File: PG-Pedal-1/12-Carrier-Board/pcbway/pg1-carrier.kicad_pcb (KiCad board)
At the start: 2 copper layers, 111 x 42.2 mm, 98 parts, among them J1 line in, J10 seed3 in + power, J11 seed3 out, J19 pg-hp, J2 line out, J20 pg-line, J3 no amp, J4 phones, J9 9V in, U1 LP2985-33, U4 NE5532, U5 NE5532, U6 NE5532, U7 TPA6139A2, U8 TPA6139A2, U9 TLV7031

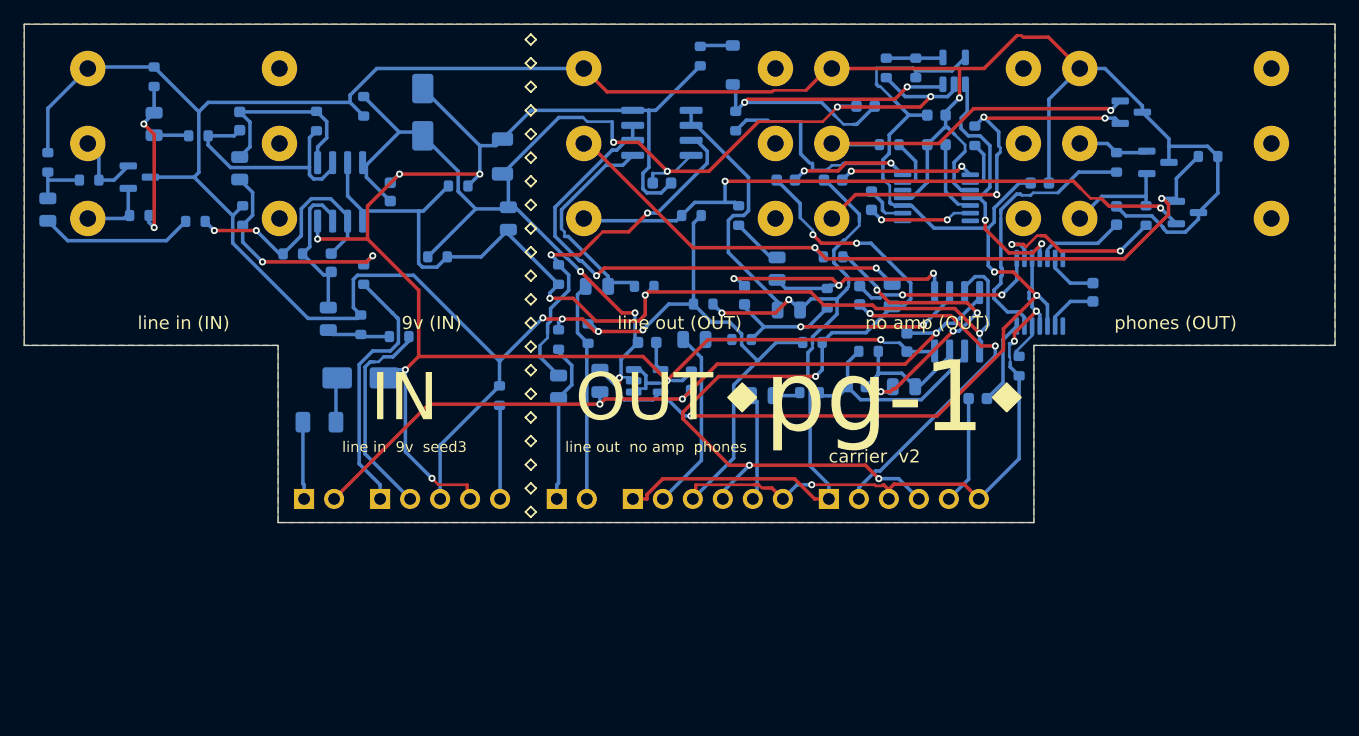
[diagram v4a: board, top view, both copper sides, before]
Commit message: v3 isolated carrier board: one isolated stereo in + out (TLV320AIC3204 behind ISO7741 / ISO1540 / B0505S), analog centre-click gain knobs, firmware SAI2 + codec, face print and drill to match
Co-Authored-By: Claude Opus 5.5 <noreply@anthropic.com>
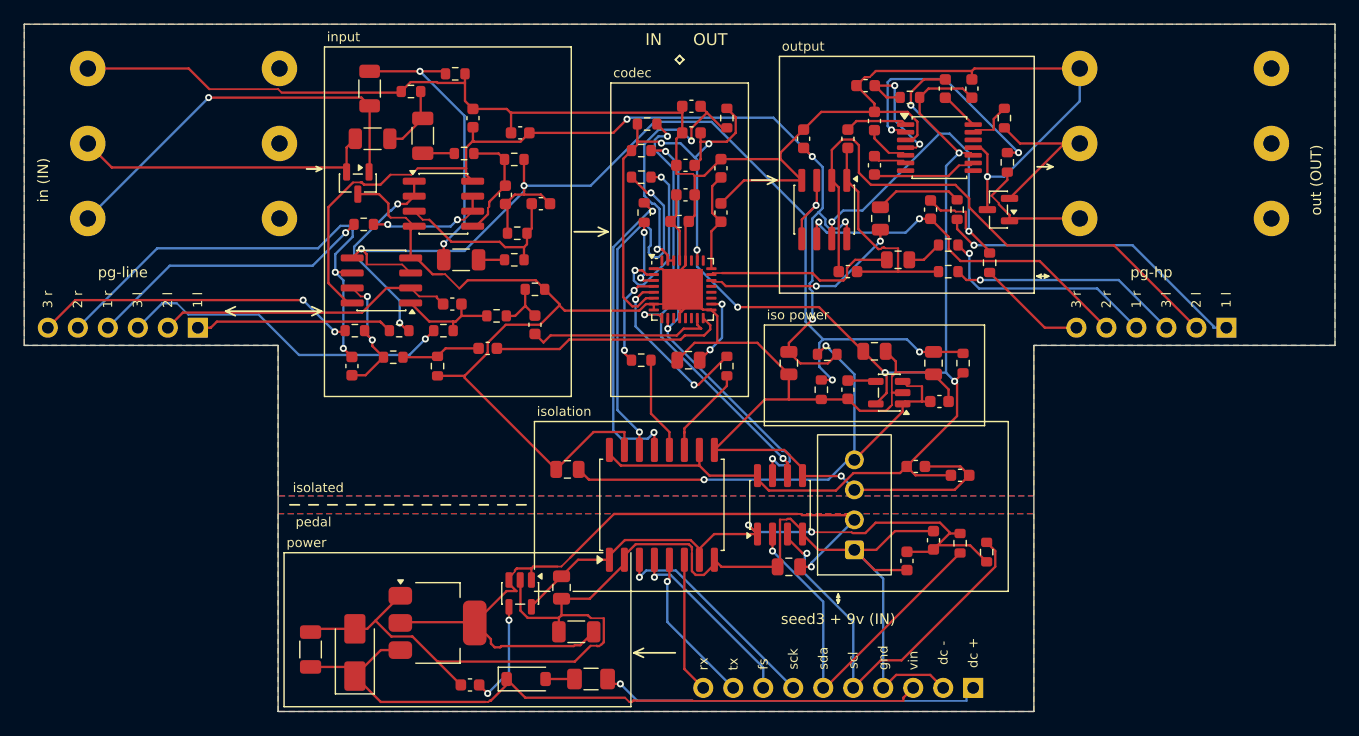
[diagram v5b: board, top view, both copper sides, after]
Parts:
- removed C34, C35, C37: 10uF 25V, C_0805_2012Metric
- removed C36: 47pF C0G, C_0603_1608Metric
- removed C38, C39, C63, C64, C65: 1uF, C_0603_1608Metric
- removed C4: 4.7uF, C_0805_2012Metric
- removed C66, C67, C68: 100nF, C_0603_1608Metric
- removed D50: 1N4148W, D_SOD-123
- removed D63, D64: PESD15VL2BT, SOT-23
- removed J11: seed3 out, PinHeader_1x02_P2.54mm_Horizontal
- removed J3: no amp, Jack_6.35mm_Neutrik_NMJ6HCD2_Horizontal
- removed J4: phones, Jack_6.35mm_Neutrik_NMJ6HCD2_Horizontal
- removed J9: 9V in, PinHeader_1x02_P2.54mm_Horizontal
- removed R1, R2: 10k, R_0603_1608Metric
- removed R15, R16, R17, R19, R21, R24, R39, R53: 100k, R_0603_1608Metric
- removed R18, R38: 51k, R_0603_1608Metric
- removed R20: 100, R_0603_1608Metric
- removed R22, R23: 1, R_0603_1608Metric
- removed R71: 0, R_0603_1608Metric
- removed U6: NE5532, SOIC-8_3.9x4.9mm_P1.27mm
- added C20: 100nF, C_0603_1608Metric, F.Cu at (103.5, 45.8)
- added C21: 1uF, C_0603_1608Metric, F.Cu at (100.0, 46.5)
- added C22: 100nF, C_0603_1608Metric, F.Cu at (100.5, 44.2)
- added C23: 1uF, C_0603_1608Metric, F.Cu at (100.5, 41.8)
- added C24: 100nF, C_0603_1608Metric, F.Cu at (101.0, 39.0)
- added C25: 100nF, C_0603_1608Metric, F.Cu at (101.0, 36.8)
- added C26: 100nF, C_0603_1608Metric, F.Cu at (82.5, 37.8)
- added C27: 100nF, C_0603_1608Metric, F.Cu at (86.5, 39.0)
- added C28: 100nF, C_0603_1608Metric, F.Cu at (110.5, 39.5)
- added C40: 47nF C0G, C_1206_3216Metric, F.Cu at (78.2, 39.2)
- added C41: 100pF C0G, C_0603_1608Metric, F.Cu at (85.2, 44.2)
- added C42: 1uF, C_0603_1608Metric, F.Cu at (83.8, 57.2)
- added C43: 100pF C0G, C_0603_1608Metric, F.Cu at (72.2, 58.8)
- added C51: 1uF, C_0603_1608Metric, F.Cu at (114.2, 39.5)
- added C52: 100pF C0G, C_0603_1608Metric, F.Cu at (114.2, 50.8)
- added C7: 10uF 25V, C_0805_2012Metric, F.Cu at (109.2, 75.8)
- added C70: 1uF, C_0603_1608Metric, F.Cu at (116.5, 41.8)
- added C71: 1uF, C_0603_1608Metric, F.Cu at (116.5, 38.0)
- added C72: 1uF, C_0603_1608Metric, F.Cu at (124.8, 35.2)
- added C73: 1uF, C_0603_1608Metric, F.Cu at (115.8, 35.0)
- added C8: 10uF 25V, C_0805_2012Metric, F.Cu at (90.5, 67.5)
- added C9: 100nF, C_0603_1608Metric, F.Cu at (119.2, 75.2)
- added R3: 4.7k, R_0603_1608Metric, F.Cu at (126.0, 74.5)
- added R4: 4.7k, R_0603_1608Metric, F.Cu at (123.8, 73.8)
- added R45: 10k, R_0603_1608Metric, F.Cu at (79.5, 58.8)
- added R46: 220, R_0603_1608Metric, F.Cu at (73.2, 46.8)
- added R47: 220, R_0603_1608Metric, F.Cu at (72.5, 55.8)
- added R5: 10, R_0603_1608Metric, F.Cu at (112.5, 57.8)
- added R6: 10k, R_0603_1608Metric, F.Cu at (124.0, 58.5)
- added R61: 1k, R_0603_1608Metric, F.Cu at (122.8, 48.5)
- added R62: 1k, R_0603_1608Metric, F.Cu at (126.2, 50.0)
- added R7: 10k, R_0603_1608Metric, F.Cu at (112.0, 60.8)
- added R8: 10k, R_0603_1608Metric, F.Cu at (104.0, 37.8)
- added R9: 4.7k, R_0603_1608Metric, F.Cu at (97.2, 38.2)
- added U10: TPA6139A2, TSSOP-14_4.4x5mm_P0.65mm, F.Cu at (122.0, 40.2)
- added U11: OPA1652, SOIC-8_3.9x4.9mm_P1.27mm, F.Cu at (74.8, 51.5)
- added U12: OPA1652, SOIC-8_3.9x4.9mm_P1.27mm, F.Cu at (112.2, 45.5)
- added U2: LP2985-33, SOT-23-5, F.Cu at (86.5, 78.0)
- added U3: B0505S-1WR3, DCDC_SIP4_B0505S, F.Cu at (114.8, 74.3)
- C1, C17, C19, C31, C61, D2, D61, D62, F1, J19, J20: moved to F.Cu
- C10, C12: value 10uF 25V -> 100nF; footprint C_0805_2012Metric -> C_0603_1608Metric; moved to F.Cu
- C11: value 100pF C0G -> 100nF; moved to F.Cu
- C13: value 10uF 25V -> 10nF; footprint C_0805_2012Metric -> C_0603_1608Metric; moved to F.Cu
- C14: value 10uF 25V -> 4.7uF; moved to F.Cu
- C15, C32: value 10uF 25V -> 1uF; footprint C_0805_2012Metric -> C_0603_1608Metric; moved to F.Cu
- C16: value 47pF C0G -> 10uF 25V; footprint C_0603_1608Metric -> C_0805_2012Metric; moved to F.Cu
- C18: value 1uF -> 10uF 25V; footprint C_0603_1608Metric -> C_0805_2012Metric; moved to F.Cu
- C2: footprint C_0805_2012Metric -> C_1206_3216Metric; moved to F.Cu
- C3: value 10nF -> 4.7uF; footprint C_0603_1608Metric -> C_0805_2012Metric; moved to F.Cu
- C30: value 10uF 25V -> 47nF C0G; footprint C_0805_2012Metric -> C_1206_3216Metric; moved to F.Cu
- C33: value 10uF 25V -> 100pF C0G; footprint C_0805_2012Metric -> C_0603_1608Metric; moved to F.Cu
- C5: value 1uF -> 10nF; moved to F.Cu
- C50, C60: value 1uF -> 4.7uF; footprint C_0603_1608Metric -> C_0805_2012Metric; moved to F.Cu
- C62: value 1uF -> 100pF C0G; moved to F.Cu
- D1: value SS34 -> B5819W; footprint D_SMA -> D_SOD-123; moved to F.Cu
- J1: value line in -> in; footprint Jack_6.35mm_Neutrik_NMJ6HCD2_Horizontal -> Jack_6.35mm_Neutrik_NMJ6HFD2_Horizontal
- J10: value seed3 in + power -> seed3 + 9v; footprint PinHeader_1x05_P2.54mm_Horizontal -> PinHeader_1x10_P2.54mm_Horizontal; moved to F.Cu
- J2: value line out -> out; footprint Jack_6.35mm_Neutrik_NMJ6HCD2_Horizontal -> Jack_6.35mm_Neutrik_NMJ6HFD2_Horizontal
- R10: value 1k -> 4.7k; moved to F.Cu
- R11: value 20k -> 33; moved to F.Cu
- R12: value 10k -> 33; moved to F.Cu
- R13: value 100 -> 33; moved to F.Cu
- R14: value 100k -> 33; moved to F.Cu
- R30: footprint R_0603_1608Metric -> R_1206_3216Metric; moved to F.Cu
- R31: value 20k -> 1M; moved to F.Cu
- R32: value 10k -> 1M; moved to F.Cu
- R33: value 100 -> 1M; moved to F.Cu
- R34, R44: value 100k -> 20k; moved to F.Cu
- R35: value 100k -> 10k; moved to F.Cu
- R36, R37: value 100k -> 220; moved to F.Cu
- R40: value 100 -> 1k; footprint R_0603_1608Metric -> R_1206_3216Metric; moved to F.Cu
- R41: value 100k -> 1M; moved to F.Cu
- R42, R43: value 1 -> 1M; moved to F.Cu
- R50: value 470k -> 1; moved to F.Cu
- R51: value 10k -> 1k; moved to F.Cu
- R52: value 100k -> 1k; moved to F.Cu
- R60: value 11.5k 1% -> 1; moved to F.Cu
- R70: value 0 -> 470k; moved to F.Cu
- U1: value LP2985-33 -> AMS1117-5.0; footprint SOT-23-5 -> SOT-223-3_TabPin2; moved to F.Cu
- U4: value NE5532 -> ISO7741; footprint SOIC-8_3.9x4.9mm_P1.27mm -> SOIC-16W_7.5x10.3mm_P1.27mm; moved to F.Cu
- U5: value NE5532 -> ISO1540; moved to F.Cu
- U7: value TPA6139A2 -> LP2985-33; footprint TSSOP-14_4.4x5mm_P0.65mm -> SOT-23-5; moved to F.Cu
- U8: value TPA6139A2 -> OPA1652; footprint TSSOP-14_4.4x5mm_P0.65mm -> SOIC-8_3.9x4.9mm_P1.27mm; moved to F.Cu
- U9: value TLV7031 -> TLV320AIC3204; footprint SOT-23-5 -> Texas_RHB0032E_VQFN-32-1EP_5x5mm_P0.5mm_EP3.45x3.45mm; moved to F.Cu
- moved C10 70.7 mm to (120.0, 67.2), turned to 0 degrees
- moved C11 68.6 mm to (121.5, 73.5)
- moved R41 67.7 mm to (77.2, 35.5), turned to 180 degrees
- moved C12 66.3 mm to (123.8, 68.0), turned to 0 degrees
- moved J10 52.7 mm to (124.9, 86.0)
- moved U8 51.1 mm to (80.0, 45.0), turned to 0 degrees
- moved R43 51.0 mm to (86.0, 41.2), turned to 0 degrees
- moved R70 46.3 mm to (119.5, 36.0), turned to 180 degrees
- moved D2 46.1 mm to (72.5, 83.0), turned to 90 degrees
- moved C1 44.8 mm to (68.8, 82.8), turned to 90 degrees
- moved R14 42.9 mm to (104.0, 58.8), turned to -90 degrees
- moved R10 42.9 mm to (96.8, 40.5)
- moved J2 42.0 mm to (133.9, 46.2)
- moved R40 40.3 mm to (74.0, 39.5), turned to 0 degrees
- moved J20 39.6 mm to (59.2, 55.5)
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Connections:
- C10 pad 1: IN_B_L -> ISO3V3
- C10 pad 2: IN_A_L -> IGND
- C11 pad 1: IN_N_L -> +3V3
- C11 pad 2: IN_O_L -> GND
- C12 pad 1: IN_O_L -> ISO3V3
- C12 pad 2: SEED_IN_RAW_L -> IGND
- C13 pad 1: OB_P_L -> IBYP
- C13 pad 2: SEED_OUT_L -> IGND
- C14 pad 1: OB_O_L -> ISO3V3
- C14 pad 2: BUS_L -> IGND
- C15 pad 1: LO_A_L -> ISO5V_RAW
- C15 pad 2: LINE_W_L -> IGND
- C16 pad 1: LO_N_L -> ISO5V
- C16 pad 2: LO_O_L -> IGND
- C17 pad 1: LO_O_L -> IBIAS
- C17 pad 2: LO_C_L -> IGND
- C18 pad 1: BUS_L -> REF
- C18 pad 2: NA_IN_L -> IGND
- C19 pad 1: HP_W_L -> AVDD
- C19 pad 2: HP_IN_L -> IGND
- C2 pad 1: VREF -> +5V
- C3 pad 1: BYP -> +3V3
- C30 pad 1: IN_B_R -> IN_A_L
- C30 pad 2: IN_A_R -> IN_B_L
- C31 pad 1: IN_N_R -> IN_C_L
- C31 pad 2: IN_O_R -> IBIAS
- C32 pad 1: IN_O_R -> IN_E_L
- C32 pad 2: SEED_IN_RAW_R -> CIN2_L
- C33 pad 1: OB_P_R -> GIN_W_L
- C33 pad 2: SEED_OUT_R -> IN_G_L
- C5 pad 1: +9V -> PBYP
- C50 pad 1: EN_RC -> LO_L
- C50 pad 2: GND -> OUT_A_L
- C60 pad 1: NA_CP -> LO_R
- C60 pad 2: NA_CN -> OUT_A_R
- C61 pad 1: AGND -> OUT_G_R
- C61 pad 2: NA_VSS -> HPIN_R
- C62 pad 1: HP_CP -> GOUT_W_R
- C62 pad 2: HP_CN -> OUT_G_R
- D61 pad 3: AGND -> IGND
- D62 pad 1: JLO_L -> JOUT_L
- D62 pad 2: JLO_R -> JOUT_R
- D62 pad 3: AGND -> IGND
- J1 pad S: AGND -> IGND
- J10 pad 1: SEED_IN_L -> +9V_RAW
- J10 pad 2: SEED_IN_R -> GND
- J10 pad 3: AGND -> +9V
- J10 pad 4: +9V -> GND
- J10 pad 5: DGND -> SEED_SCL
- J19 pad 1: BUS_L -> GOUT_A_L
- J19 pad 2: HP_W_L -> GOUT_W_L
- J19 pad 3: AGND -> GOUT_B_L
- J19 pad 4: BUS_R -> GOUT_A_R
- J19 pad 5: HP_W_R -> GOUT_W_R
- J19 pad 6: AGND -> GOUT_B_R
- J2 pad R: JLO_R -> JOUT_R
- J2 pad S: AGND -> IGND
- J2 pad T: JLO_L -> JOUT_L
- J20 pad 1: BUS_L -> GIN_A_L
- J20 pad 2: LINE_W_L -> GIN_W_L
- J20 pad 3: AGND -> GIN_B_L
- J20 pad 4: BUS_R -> GIN_A_R
- J20 pad 5: LINE_W_R -> GIN_W_R
- J20 pad 6: AGND -> GIN_B_R
- R10 pad 1: JIN_L -> ISO3V3
- R10 pad 2: IN_A_L -> ISDA
- R11 pad 1: IN_B_L -> BCLK_X
- R11 pad 2: IN_N_L -> BCLK
- R12 pad 1: IN_N_L -> WCLK_X
- R12 pad 2: IN_O_L -> WCLK
- R13 pad 1: SEED_IN_RAW_L -> DIN_X
- R13 pad 2: SEED_IN_L -> DIN
- R14 pad 1: SEED_IN_RAW_L -> DOUT
- R14 pad 2: AGND -> DOUT_X
- R30 pad 1: JIN_R -> JIN_L
- R30 pad 2: IN_A_R -> IN_A_L
- R31 pad 1: IN_B_R -> IN_A_L
- R31 pad 2: IN_N_R -> IGND
- R32 pad 1: IN_N_R -> IN_B_L
- R32 pad 2: IN_O_R -> IN_C_L
- R33 pad 1: SEED_IN_RAW_R -> IN_C_L
- R33 pad 2: SEED_IN_R -> IBIAS
- R34 pad 1: SEED_IN_RAW_R -> IN_G_L
- R34 pad 2: AGND -> IN_E_L
- R35 pad 1: OB_P_R -> IN_E_L
- R35 pad 2: VREF -> IGND
- R36 pad 1: SEED_OUT_R -> IN_D_L
- R36 pad 2: AGND -> GIN_A_L
- R37 pad 1: BUS_R -> GIN_B_L
- R37 pad 2: AGND -> IN_G_L
- R40 pad 1: LO_C_R -> JIN_R
- R40 pad 2: JLO_R -> IN_A_R
- R41 pad 1: JLO_R -> IN_A_R
- R41 pad 2: AGND -> IGND
- R42 pad 1: NA_O_R -> IN_B_R
- R42 pad 2: JNA_R -> IN_C_R
- R43 pad 1: HP_O_R -> IN_C_R
- R43 pad 2: JHP_R -> IBIAS
- R44 pad 1: IN_A_R -> IN_G_R
- R44 pad 2: AGND -> IN_E_R
- R50 pad 1: +3V3A -> HPO_L
- R50 pad 2: EN_RC -> JOUT_L
- R51 pad 1: +9V -> OUT_A_L
- R51 pad 2: +9V_SENSE -> GOUT_A_L
- R52 pad 1: +3V3A -> GOUT_B_L
- R52 pad 2: EN_REF -> OUT_G_L
- R60 pad 1: HP_GAIN -> HPO_R
- R60 pad 2: AGND -> JOUT_R
- R70 pad 1: GND -> ISO3V3
- R70 pad 2: AGND -> HP_ON
- U1 pad 1: +9V -> GND
- U1 pad 2: GND -> +5V
- U4 pad 1: IN_O_L -> +3V3
- U4 pad 2: IN_N_L -> GND
- U4 pad 3: VREF -> SEED_SCK
- U4 pad 4: GND -> SEED_FS
- U4 pad 5: VREF -> SEED_TX
- U4 pad 6: IN_N_R -> SEED_RX
- U4 pad 7: IN_O_R -> +3V3
- U4 pad 8: +9V -> GND
- U5 pad 1: OB_O_L -> +3V3
- U5 pad 2: OB_O_L -> SEED_SDA
- U5 pad 3: OB_P_L -> SEED_SCL
- U5 pad 5: OB_P_R -> IGND
- U5 pad 6: OB_O_R -> ISCL
- U5 pad 7: OB_O_R -> ISDA
- U5 pad 8: +9V -> ISO3V3
- U7 pad 1: NA_IN_L -> ISO5V_RAW
- U7 pad 2: NA_O_L -> IGND
- U7 pad 3: AGND -> ISO5V_RAW
- U7 pad 4: MUTE_N -> IBYP
- U7 pad 5: NA_VSS -> ISO3V3
- U8 pad 1: HP_IN_L -> IN_D_L
- U8 pad 2: HP_O_L -> IN_D_L
- U8 pad 3: AGND -> IN_C_L
- U8 pad 4: MUTE_N -> IGND
- U8 pad 5: HP_VSS -> IN_C_R
- U8 pad 6: HP_CN -> IN_D_R
- U8 pad 7: (no net) -> IN_D_R
- U8 pad 8: (no net) -> ISO5V
- U9 pad 1: MUTE_N -> IGND
- U9 pad 2: GND -> BCLK
- U9 pad 3: EN_RC -> WCLK
- U9 pad 4: EN_REF -> DIN
- U9 pad 5: +3V3A -> DOUT
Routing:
- net AGND: track 336.9 -> 0.00 mm, vias 8 -> 0
- net IGND: track 0.00 -> 300.6 mm, vias 0 -> 2
- net ISO3V3: track 0.00 -> 148.1 mm, vias 0 -> 7
- net +3V3A: track 112.0 -> 0.00 mm, vias 3 -> 0
- net IBIAS: track 0.00 -> 97.5 mm, vias 0 -> 5
- net ISO5V: track 0.00 -> 87.3 mm, vias 0 -> 4
- net +9V: track 146.5 -> 59.4 mm, vias 7 -> 0
- net VREF: track 85.8 -> 0.00 mm, vias 3 -> 0
- net BUS_R: track 69.0 -> 0.00 mm, vias 5 -> 0
- net GND: track 181.9 -> 114.7 mm, vias 10 -> 0
- net JLO_R: track 63.8 -> 0.00 mm, vias 2 -> 0
- net +5V: track 0.00 -> 63.3 mm, vias 0 -> 1
- net BUS_L: track 62.3 -> 0.00 mm, vias 2 -> 0
- net JLO_L: track 55.5 -> 0.00 mm, vias 2 -> 0
- net +3V3: track 0.00 -> 52.8 mm, vias 0 -> 2
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- added copper zone on B.Cu, net GND
- added copper zone on F.Cu, net GND
- added copper zone on B.Cu, net IGND
- added copper zone on F.Cu, net IGND
- removed copper zone on B.Cu, net AGND
- removed copper zone on F.Cu, net AGND
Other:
- board size 111 x 42.2 mm -> 111 x 58.2 mm
- board text added: "1 l"
- board text added: "1 r"
- board text added: "2 l"
- board text added: "2 r"
- board text added: "3 l"
- board text added: "3 r"
- board text added: "codec"
- board text added: "dc +"
- board text added: "dc -"
- board text added: "fs"
- board text added: "in (IN)"
- board text added: "input"
- board text added: "iso power"
- board text added: "isolated"
- board text added: "isolation"
- board text added: "out (OUT)"
- board text added: "output"
- board text added: "pedal"
- board text added: "power"
- board text added: "rx"
- board text added: "sck"
- board text added: "scl"
- board text added: "sda"
- board text added: "seed3 + 9v (IN)"
- board text added: "tx"
- board text added: "vin"
- board text removed: "+"
- board text removed: "-"
- board text removed: "9v"
- board text removed: "9v (IN)"
- board text removed: "agnd"
- board text removed: "bus l"
- board text removed: "bus r"
- board text removed: "carrier v2"
- board text removed: "dgnd"
- board text removed: "hp l"
- board text removed: "hp r"
- board text removed: "in l"
- board text removed: "in r"
- board text removed: "line in (IN)"
- board text removed: "line in 9v seed3"
- board text removed: "line l"
- board text removed: "line out (OUT)"
- board text removed: "line out no amp phones"
- board text removed: "line r"
- board text removed: "no amp (OUT)"
- board text removed: "out l"
- board text removed: "out r"
- board text removed: "pg-1"
- board text removed: "phones (OUT)"
- board text removed: "seed3 (IN)"
- board text removed: "seed3 (OUT)"

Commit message: Carrier: analog fx (MCP4461 level + low-pass, TLV9062), expansion header + left-wall bay, re-route
Co-Authored-By: Claude Opus 5.5 <noreply@anthropic.com>
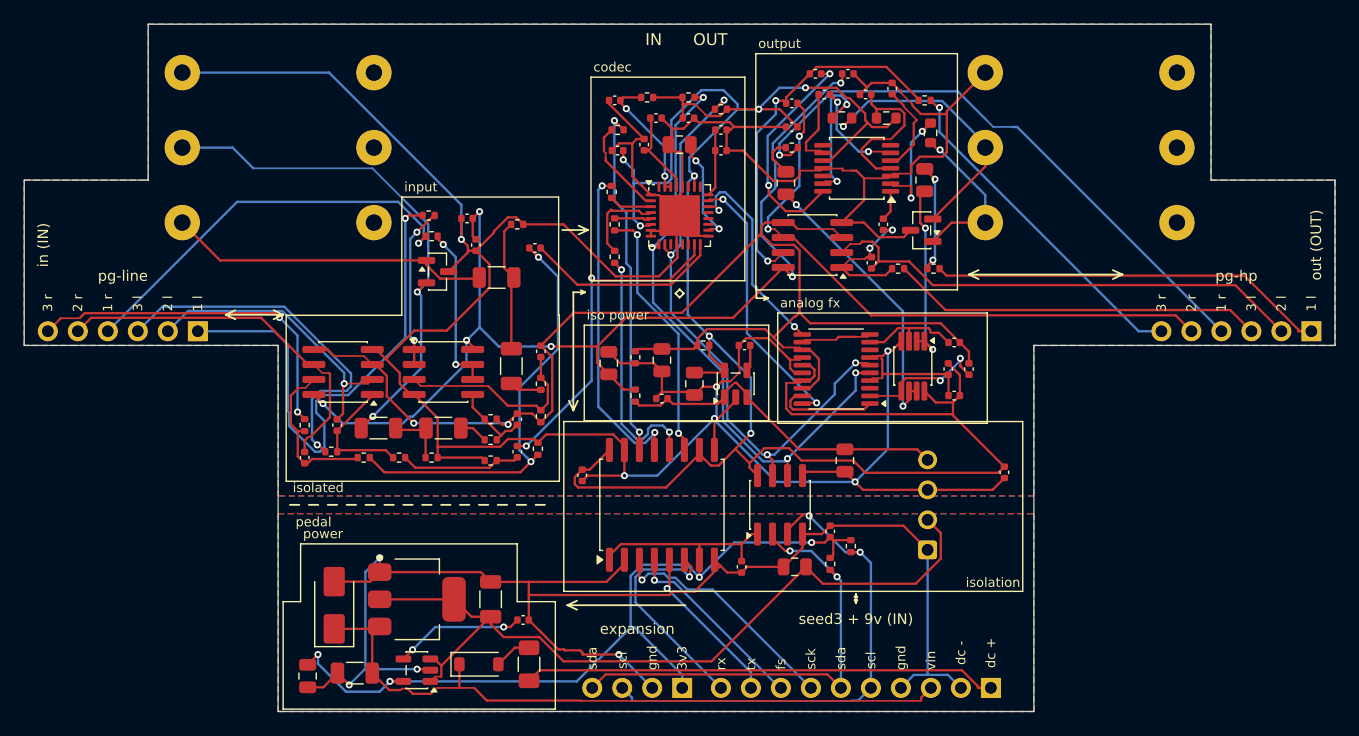
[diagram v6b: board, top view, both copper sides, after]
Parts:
- added C74: 10nF C0G, C_0402_1005Metric, F.Cu at (123.2, 56.8)
- added C75: 100nF, C_0402_1005Metric, F.Cu at (122.8, 59.0)
- added C76: 10nF C0G, C_0402_1005Metric, F.Cu at (124.5, 59.0)
- added C78: 100nF, C_0402_1005Metric, F.Cu at (123.2, 61.2)
- added J21: expansion, PinHeader_1x04_P2.54mm_Horizontal, F.Cu at (100.2, 86.0)
- added U13: MCP4461-103, TSSOP-20_4.4x6.5mm_P0.65mm, F.Cu at (113.2, 59.0)
- added U15: TLV9062, VSSOP-8_3x3mm_P0.65mm, F.Cu at (119.8, 58.8)
- C10, C11, C12, C13, C15, C19, C20, C21, C22, C23, C24, C25, C26, C27, C28, C31, C32, C33, C41, C42, C43, C5, C51, C52, C61, C62, C70, C71, C72, C73, C9: footprint C_0603_1608Metric -> C_0402_1005Metric
- R10, R11, R12, R13, R14, R3, R31, R32, R33, R34, R35, R36, R37, R4, R41, R42, R43, R44, R45, R46, R47, R5, R51, R52, R6, R61, R62, R7, R8, R9: footprint R_0603_1608Metric -> R_0402_1005Metric
- moved R41 31.0 mm to (79.0, 66.5), turned to 0 degrees
- moved C10 28.3 mm to (91.8, 68.0), turned to -90 degrees
- moved C40 24.8 mm to (80.0, 64.0), turned to 0 degrees
- moved R40 24.5 mm to (74.5, 64.0)
- moved R42 24.4 mm to (84.0, 65.0)
- moved C8 23.5 mm to (114.0, 66.8), turned to -90 degrees
- moved C15 23.5 mm to (98.5, 61.5), turned to 180 degrees
- moved C17 23.0 mm to (98.5, 58.2)
- moved C3 22.8 mm to (68.5, 85.0)
- moved R43 22.1 mm to (84.0, 63.2)
- moved R6 22.1 mm to (102.0, 57.0), turned to 180 degrees
- moved R30 19.3 mm to (84.5, 51.2), turned to 0 degrees
- moved C41 19.0 mm to (86.2, 63.2), turned to 90 degrees
- moved C18 18.3 mm to (100.0, 40.0)
- moved R5 16.6 mm to (96.2, 61.2), turned to 90 degrees
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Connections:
- C50 pad 1: LO_L -> ABUF_L
- C60 pad 1: LO_R -> ABUF_R
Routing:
- net ISO3V3: track 148.1 -> 182.8 mm
- net +3V3: track 52.8 -> 84.9 mm, vias 2 -> 4
- net GOUT_A_R: track 19.3 -> 50.5 mm
- net IN_E_R: track 6.71 -> 36.2 mm, vias 0 -> 2
- net GIN_A_L: track 16.8 -> 44.7 mm, vias 0 -> 1
- net ABUF_R: track 0.00 -> 24.2 mm, vias 0 -> 2
- net GOUT_W_R: track 31.3 -> 51.6 mm
- net GOUT_B_R: track 9.29 -> 28.9 mm, vias 0 -> 1
- net ISO5V_RAW: track 48.0 -> 29.2 mm, vias 2 -> 0
- net JIN_R: track 25.9 -> 44.5 mm, vias 0 -> 2
- net HPIN_R: track 3.30 -> 19.0 mm, vias 0 -> 2
- net ABUF_L: track 0.00 -> 15.6 mm, vias 0 -> 2
- net ISDA: track 36.9 -> 52.2 mm, vias 3 -> 4
- net IBIAS: track 97.5 -> 112.8 mm, vias 5 -> 2
- net DOUT_X: track 7.76 -> 21.9 mm, vias 0 -> 2
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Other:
- outline, holes or cut-outs redrawn
- board text added: "3v3"
- board text added: "analog fx"
- board text added: "expansion"

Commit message: Carrier: cheaper isolated board (fx loop header instead of analog fx, basic-part clamps), all parts fitted
Co-Authored-By: Claude Opus 5.5 <noreply@anthropic.com>
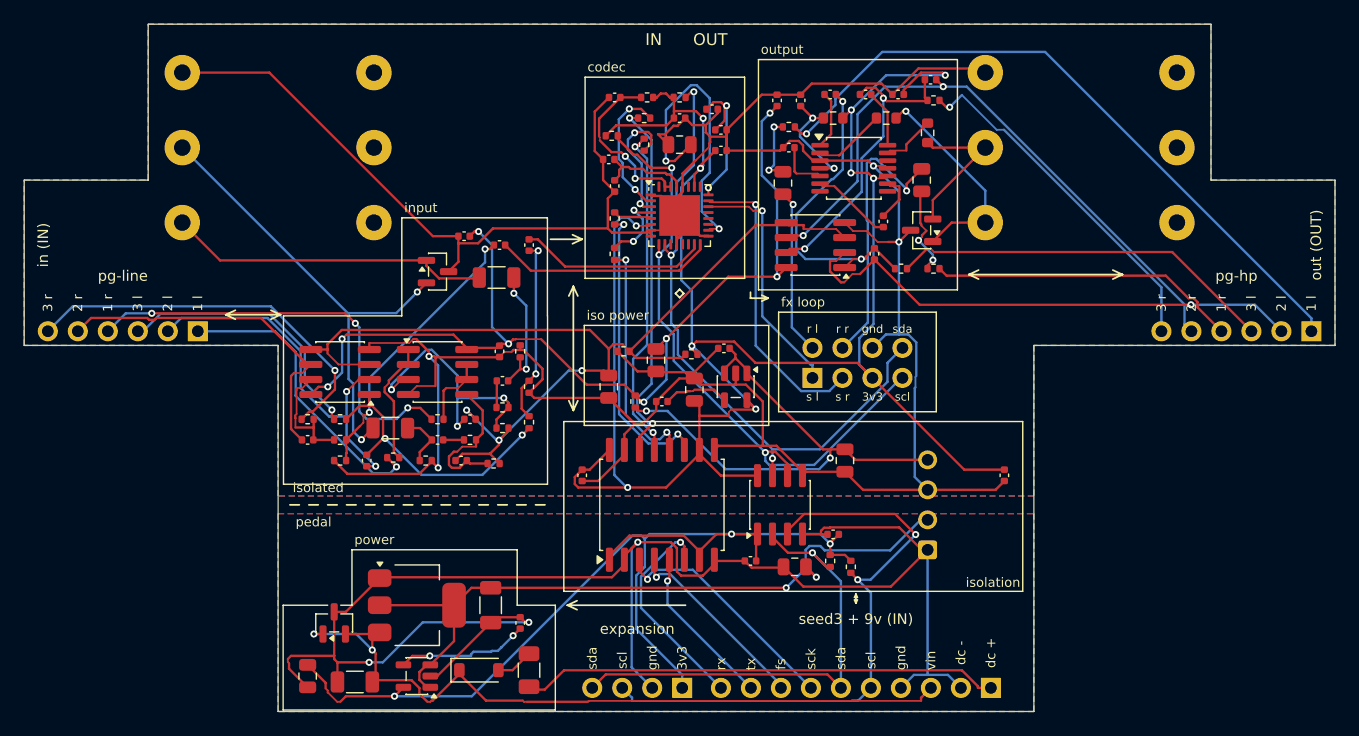
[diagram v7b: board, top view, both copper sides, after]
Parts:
- removed C74, C76: 10nF C0G, C_0402_1005Metric
- removed C75, C78: 100nF, C_0402_1005Metric
- removed U13: MCP4461-103, TSSOP-20_4.4x6.5mm_P0.65mm
- removed U15: TLV9062, VSSOP-8_3x3mm_P0.65mm
- added J22: fx loop, PinHeader_2x04_P2.54mm_Vertical, F.Cu at (111.2, 59.8)
- C30, C40: value 47nF C0G -> 100nF; footprint C_1206_3216Metric -> C_0402_1005Metric
- D2: value SMAJ12A -> PSM712; footprint D_SMA -> SOT-23
- D61, D62: value PESD15VL2BT -> PSM712
- moved R36 20.7 mm to (75.8, 66.5)
- moved C32 17.5 mm to (87.2, 48.5)
- moved R51 17.1 mm to (109.2, 38.5)
- moved R45 16.8 mm to (71.2, 66.8), turned to 180 degrees
- moved R61 15.8 mm to (121.5, 50.5)
- moved R46 15.5 mm to (79.5, 63.2)
- moved C50 12.0 mm to (108.8, 43.2)
- moved C62 11.9 mm to (121.2, 34.5)
- moved C51 11.9 mm to (112.8, 35.8), turned to 180 degrees
- moved C70 11.9 mm to (117.2, 46.5), turned to -90 degrees
- moved C60 11.5 mm to (120.5, 43.0), turned to -90 degrees
- moved R34 11.4 mm to (87.2, 63.5), turned to 90 degrees
- moved R31 10.8 mm to (86.5, 57.5), turned to 90 degrees
- moved C71 10.1 mm to (109.2, 40.2), turned to 0 degrees
- moved C72 9.41 mm to (118.5, 35.8)
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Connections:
- C50 pad 1: ABUF_L -> FXR_L
- C60 pad 1: ABUF_R -> FXR_R
- D2 pad 2: GND -> +9V
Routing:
- net IBIAS: track 112.8 -> 88.5 mm, vias 2 -> 3
- net ABUF_R: track 24.2 -> 0.00 mm, vias 2 -> 0
- net GOUT_A_R: track 50.5 -> 26.3 mm, vias 1 -> 0
- net GOUT_A_L: track 33.8 -> 57.6 mm, vias 0 -> 1
- net FXR_R: track 0.00 -> 23.7 mm, vias 0 -> 1
- net IGND: track 313.3 -> 290.6 mm, vias 6 -> 4
- net GND: track 120.9 -> 142.0 mm, vias 4 -> 3
- net GIN_A_L: track 44.7 -> 25.3 mm
- net REF: track 9.07 -> 24.9 mm
- net ABUF_L: track 15.6 -> 0.00 mm, vias 2 -> 0
- net OUT_G_L: track 11.8 -> 26.7 mm
- net HPIN_R: track 19.0 -> 4.87 mm, vias 2 -> 0
- net FXR_L: track 0.00 -> 14.1 mm, vias 0 -> 1
- net ISO5V_RAW: track 29.2 -> 42.5 mm, vias 0 -> 2
- net IN_G_L: track 11.1 -> 24.0 mm, vias 0 -> 2
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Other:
- board text added: "fx loop"
- board text added: "r l"
- board text added: "r r"
- board text added: "s l"
- board text added: "s r"
- board text removed: "analog fx"

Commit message: Carrier: ~$50 build (TLV9062, XC6206 basic parts, through-hole parts hand-soldered)
Co-Authored-By: Claude Opus 5.5 <noreply@anthropic.com>
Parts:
- removed C13, C5: 10nF, C_0402_1005Metric
- U11, U12, U8: value OPA1652 -> TLV9062
- U2, U7: value LP2985-33 -> XC6206P332MR; footprint SOT-23-5 -> SOT-23
- moved R43 18.5 mm to (83.2, 48.5), turned to 90 degrees
- moved C42 18.0 mm to (84.8, 66.5)
- moved R61 14.3 mm to (121.2, 36.2)
- moved R62 14.3 mm to (121.2, 50.5)
- moved C32 13.8 mm to (88.5, 62.2)
- moved C51 11.6 mm to (117.0, 46.5), turned to 90 degrees
- moved R45 10.8 mm to (82.0, 66.8), turned to 0 degrees
- moved C70 9.96 mm to (109.5, 40.2), turned to 180 degrees
- moved C71 9.86 mm to (117.8, 35.2), turned to -90 degrees
- moved C23 9.49 mm to (94.5, 43.5), turned to 90 degrees
- moved D2 9.40 mm to (79.0, 85.0), turned to 0 degrees
- moved R31 9.03 mm to (85.8, 48.5)
- moved C72 8.31 mm to (110.2, 36.8)
- moved R46 8.25 mm to (71.2, 63.2)
- moved U2 8.13 mm to (72.0, 79.2), turned to -90 degrees
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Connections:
- U2 pad 1: +5V -> GND
- U2 pad 2: GND -> +3V3
- U7 pad 1: ISO5V_RAW -> IGND
- U7 pad 2: IGND -> ISO3V3
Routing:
- net ISO3V3: track 177.5 -> 127.8 mm, vias 10 -> 5
- net IGND: track 290.6 -> 314.6 mm, vias 4 -> 8
- net IN_G_R: track 9.96 -> 30.0 mm, vias 0 -> 2
- net IN_E_R: track 23.9 -> 7.69 mm
- net REF: track 24.9 -> 9.07 mm
- net ISO5V_RAW: track 42.5 -> 28.3 mm
- net OUT_G_L: track 26.7 -> 12.8 mm
- net IN_C_R: track 12.3 -> 24.7 mm, vias 0 -> 3
- net IN_C_L: track 22.1 -> 10.4 mm, vias 3 -> 0
- net IN_E_L: track 15.6 -> 4.31 mm, vias 2 -> 0
- net PBYP: track 11.2 -> 0.00 mm, vias 2 -> 0
- net OUT_G_R: track 25.6 -> 35.7 mm
- net CIN2_R: track 18.6 -> 27.7 mm, vias 0 -> 2
- net GIN_A_R: track 36.7 -> 27.6 mm, vias 3 -> 1
- net HP_CN: track 6.89 -> 15.8 mm, vias 0 -> 2
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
